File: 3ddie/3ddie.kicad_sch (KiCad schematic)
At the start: 55 parts, among them J1 USB4105-GF-A, J2 TRS_MIDI_IN, J3 TRS_MIDI_OUT, U1 W25Q128JV, U2 RP2040, U3 MCP1702T-3302E_CB, U4 MGC3130-I/MQ, U5 MCP1416R, U6 6N137, U7 BoostedElectrodes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

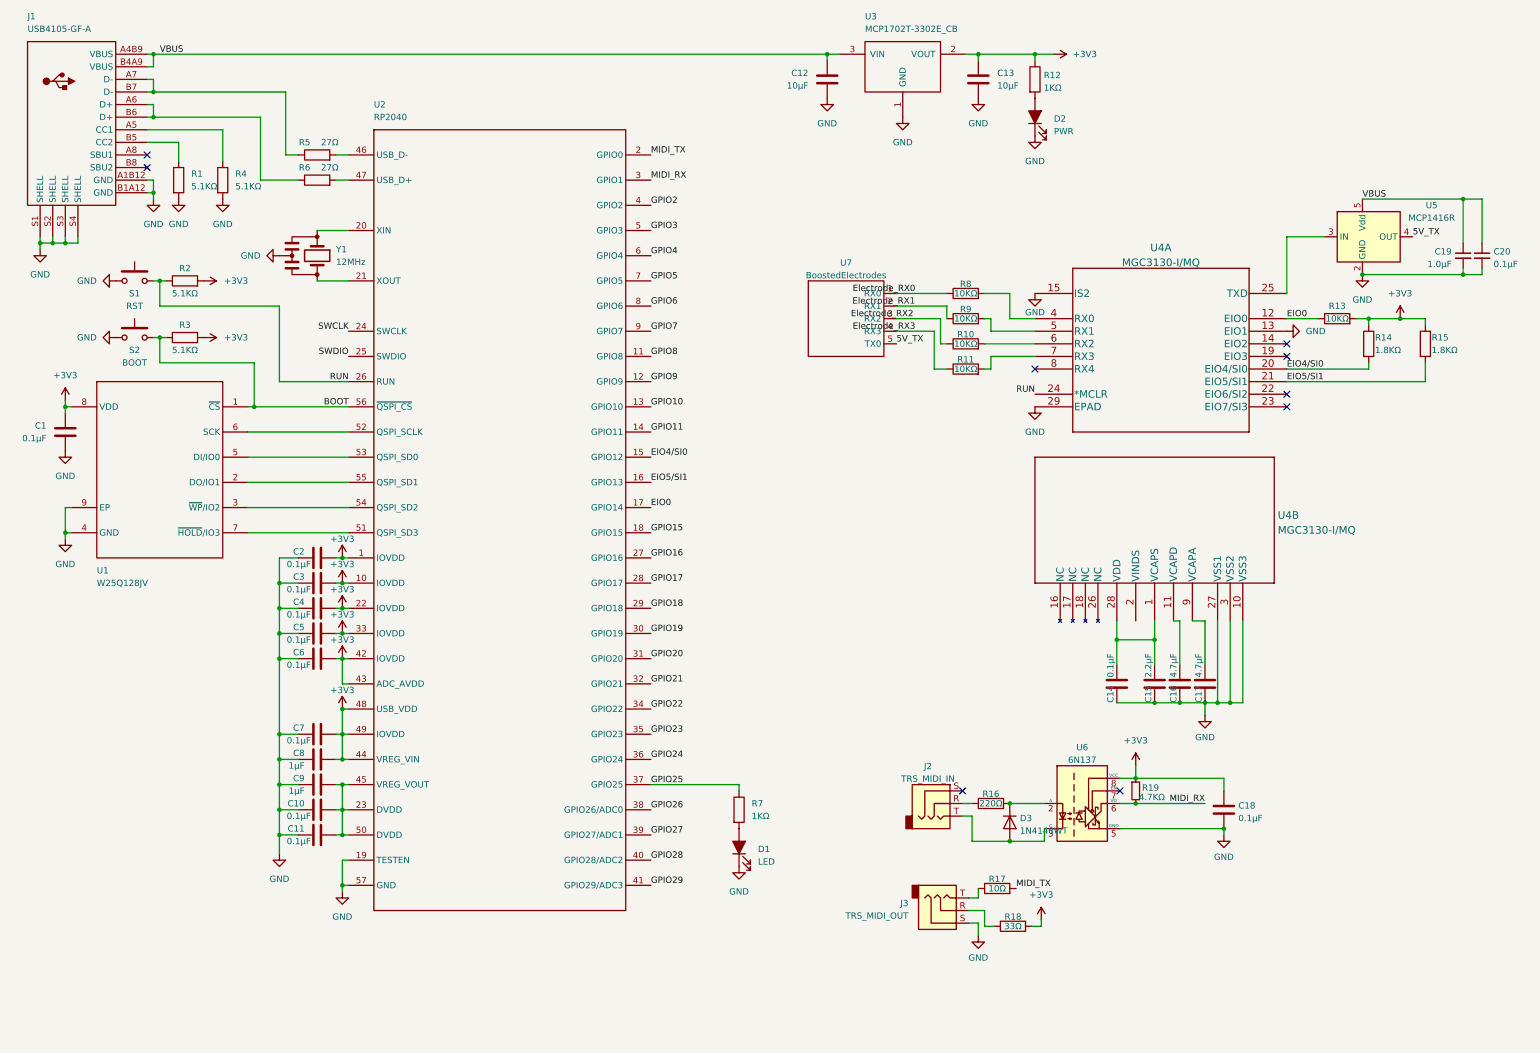
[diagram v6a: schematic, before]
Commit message: Adding pots, pin sockets, and footprints
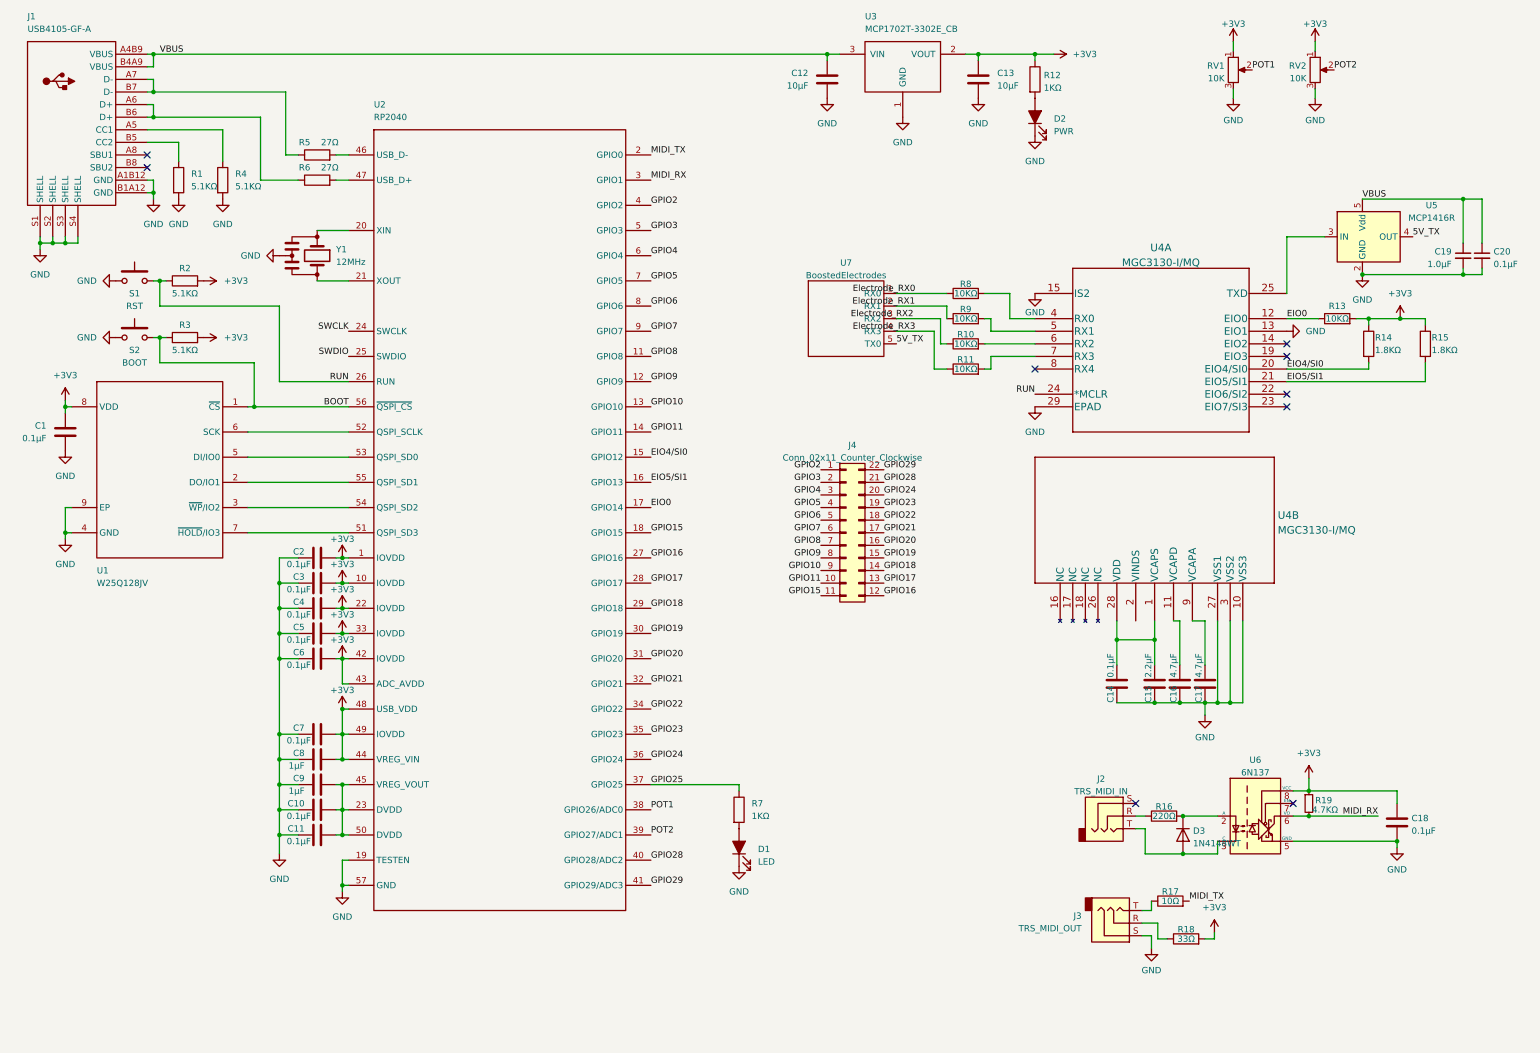
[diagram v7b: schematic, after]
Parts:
- added J4: Conn_02x11_Counter_Clockwise, Connector_PinSocket_2.54mm:PinSocket_2x11_P2.54mm_Horizontal, symbol Connector_Generic:Conn_02x11_Counter_Clockwise
- added RV1, RV2: 10K, 3ddie:PDB12-H4251-103BF, symbol Device:R_Potentiometer
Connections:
- net +3V3: now also RV1.1, RV2.1
- net GND: now also RV1.3, RV2.3
- net GPIO10: now also J4.9 (Pin_9)
- net GPIO11: now also J4.10 (Pin_10)
- net GPIO15: now also J4.11 (Pin_11)
- net GPIO16: now also J4.12 (Pin_12)
- net GPIO17: now also J4.13 (Pin_13)
- net GPIO18: now also J4.14 (Pin_14)
- net GPIO19: now also J4.15 (Pin_15)
- net GPIO2: now also J4.1 (Pin_1)
- net GPIO20: now also J4.16 (Pin_16)
- net GPIO21: now also J4.17 (Pin_17)
- net GPIO22: now also J4.18 (Pin_18)
- net GPIO23: now also J4.19 (Pin_19)
- net GPIO24: now also J4.20 (Pin_20)
- net GPIO28: now also J4.21 (Pin_21)
- net GPIO29: now also J4.22 (Pin_22)
- net GPIO3: now also J4.2 (Pin_2)
- net GPIO4: now also J4.3 (Pin_3)
- net GPIO5: now also J4.4 (Pin_4)
- net GPIO6: now also J4.5 (Pin_5)
- net GPIO7: now also J4.6 (Pin_6)
- net GPIO8: now also J4.7 (Pin_7)
- net GPIO9: now also J4.8 (Pin_8)
- net GPIO26 renamed POT1
- net POT1: now also RV1.2
- net GPIO27 renamed POT2
- net POT2: now also RV2.2
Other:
- moved on the sheet: C18, D3, J2, J3, R16, R17, R18, R19, U6
